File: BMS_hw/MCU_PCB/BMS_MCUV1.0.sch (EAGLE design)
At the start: 37 parts, among them IC2 SST25VF020B804ISA, Q1 CRYSTALS-GND-LID-IQXC-42

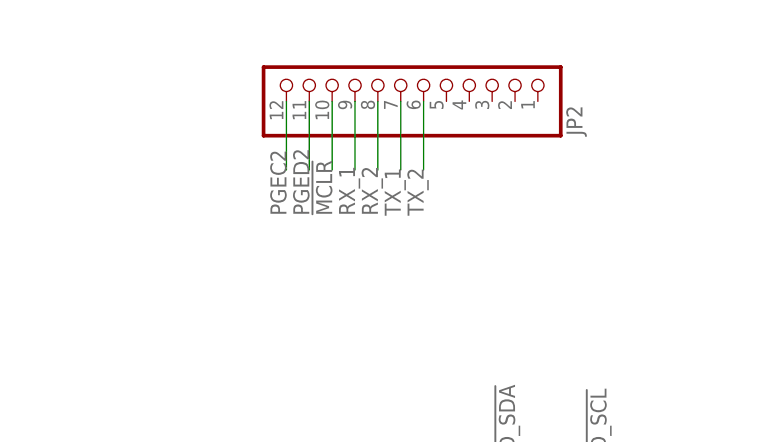
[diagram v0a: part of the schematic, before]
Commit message: afe mcu schematic updated
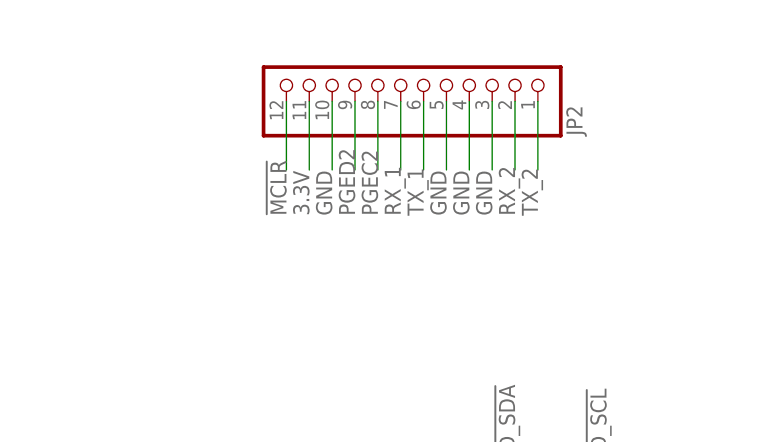
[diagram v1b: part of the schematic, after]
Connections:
- net !MCLR: now also JP2.12; no longer JP2.10
- net 3.3V: now also JP2.11
- net GND: now also JP2.10, JP2.3, JP2.4, JP2.5
- net PGEC2: now also JP2.8; no longer JP2.12
- net PGED2: now also JP2.9; no longer JP2.11
- net RX_1: now also JP2.7; no longer JP2.9
- net RX_2: now also JP2.2; no longer JP2.8
- net TX_1: now also JP2.6; no longer JP2.7
- net TX_2: now also JP2.1; no longer JP2.6
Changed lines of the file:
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@@
 <pinref part="GND13" gate="1" pin="GND"/>
+</segment>
+<segment>
+<pinref part="JP2" gate="G$1" pin="10"/>
+<wire x1="317.5" y1="243.84" x2="317.5" y2="236.22" width="0.1524" layer="91"/>
+<label x="317.5" y="231.14" size="1.778" layer="95" font="vector" ratio="12" rot="R90"/>
+</segment>
+<segment>
+<pinref part="JP2" gate="G$1" pin="5"/>
+<wire x1="330.2" y1="243.84" x2="330.2" y2="236.22" width="0.1524" layer="91"/>
+<label x="330.2" y="231.14" size="1.778" layer="95" rot="R90"/>
+</segment>
+<segment>
+<pinref part="JP2" gate="G$1" pin="4"/>
+<wire x1="332.74" y1="243.84" x2="332.74" y2="236.22" width="0.1524" layer="91"/>
+<label x="332.74" y="231.14" size="1.778" layer="95" rot="R90"/>
+</segment>
+<segment>
+<pinref part="JP2" gate="G$1" pin="3"/>
+<wire x1="335.28" y1="243.84" x2="335.28" y2="236.22" width="0.1524" layer="91"/>
+<label x="335.28" y="231.14" size="1.778" layer="95" rot="R90"/>
 </segment>
 </net>
@@
 <wire x1="228.6" y1="210.82" x2="220.98" y2="210.82" width="0.1524" layer="91"/>
 <label x="215.9" y="210.82" size="1.778" layer="95" font="vector" ratio="12"/>
+</segment>
+<segment>
+<pinref part="JP2" gate="G$1" pin="11"/>
+<wire x1="314.96" y1="243.84" x2="314.96" y2="236.22" width="0.1524" layer="91"/>
+<label x="314.96" y="231.14" size="1.778" layer="95" font="vector" ratio="12" rot="R90"/>
 </segment>
 </net>
@@
 </segment>
 <segment>
-<pinref part="JP2" gate="G$1" pin="10"/>
-<wire x1="317.5" y1="243.84" x2="317.5" y2="236.22" width="0.1524" layer="91"/>
-<label x="317.5" y="231.14" size="1.778" layer="95" font="vector" ratio="12" rot="R90"/>
+<pinref part="JP2" gate="G$1" pin="12"/>
+<wire x1="312.42" y1="243.84" x2="312.42" y2="236.22" width="0.1524" layer="91"/>
+<label x="312.42" y="231.14" size="1.778" layer="95" font="vector" ratio="12" rot="R90"/>
 </segment>
 </net>
@@
 </segment>
 <segment>
-<pinref part="JP2" gate="G$1" pin="9"/>
-<wire x1="320.04" y1="243.84" x2="320.04" y2="236.22" width="0.1524" layer="91"/>
-<label x="320.04" y="231.14" size="1.778" layer="95" font="vector" ratio="12" rot="R90"/>
+<pinref part="JP2" gate="G$1" pin="7"/>
+<wire x1="325.12" y1="243.84" x2="325.12" y2="236.22" width="0.1524" layer="91"/>
+<label x="325.12" y="231.14" size="1.778" layer="95" font="vector" ratio="12" rot="R90"/>
 </segment>
 </net>
@@
 </segment>
 <segment>
+<pinref part="JP2" gate="G$1" pin="1"/>
+<wire x1="340.36" y1="243.84" x2="340.36" y2="236.22" width="0.1524" layer="91"/>
+<label x="340.36" y="231.14" size="1.778" layer="95" rot="R90"/>
+</segment>
+</net>
+<net name="N$73" class="0">
+<segment>
+<pinref part="MCU2" gate="G$1" pin="OA3IN+/AN8/C3IN1+/C3IN3-/RPC2/PMA13/RC2"/>
+<wire x1="35.56" y1="157.48" x2="33.02" y2="157.48" width="0.1524" layer="91"/>
+</segment>
+</net>
+<net name="TX_1" class="0">
+<segment>
+<pinref part="MCU2" gate="G$1" pin="RPB15/PMD7/RB15"/>
+<wire x1="35.56" y1="170.18" x2="33.02" y2="170.18" width="0.1524" layer="91"/>
+<label x="27.94" y="170.18" size="1.778" layer="95" font="vector" ratio="12"/>
+</segment>
+<segment>
 <pinref part="JP2" gate="G$1" pin="6"/>
 <wire x1="327.66" y1="243.84" x2="327.66" y2="236.22" width="0.1524" layer="91"/>
 <label x="327.66" y="231.14" size="1.778" layer="95" font="vector" ratio="12" rot="R90"/>
-</segment>
-</net>
-<net name="N$73" class="0">
-<segment>
-<pinref part="MCU2" gate="G$1" pin="OA3IN+/AN8/C3IN1+/C3IN3-/RPC2/PMA13/RC2"/>
-<wire x1="35.56" y1="157.48" x2="33.02" y2="157.48" width="0.1524" layer="91"/>
-</segment>
-</net>
-<net name="TX_1" class="0">
-<segment>
-<pinref part="MCU2" gate="G$1" pin="RPB15/PMD7/RB15"/>
-<wire x1="35.56" y1="170.18" x2="33.02" y2="170.18" width="0.1524" layer="91"/>
-<label x="27.94" y="170.18" size="1.778" layer="95" font="vector" ratio="12"/>
-</segment>
-<segment>
-<pinref part="JP2" gate="G$1" pin="7"/>
-<wire x1="325.12" y1="243.84" x2="325.12" y2="236.22" width="0.1524" layer="91"/>
-<label x="325.12" y="231.14" size="1.778" layer="95" font="vector" ratio="12" rot="R90"/>
 </segment>
 </net>
@@
 </segment>
 <segment>
-<pinref part="JP2" gate="G$1" pin="12"/>
-<wire x1="312.42" y1="243.84" x2="312.42" y2="236.22" width="0.1524" layer="91"/>
-<label x="312.42" y="231.14" size="1.778" layer="95" font="vector" ratio="12" rot="R90"/>
+<pinref part="JP2" gate="G$1" pin="8"/>
+<wire x1="322.58" y1="243.84" x2="322.58" y2="236.22" width="0.1524" layer="91"/>
+<label x="322.58" y="231.14" size="1.778" layer="95" font="vector" ratio="12" rot="R90"/>
 </segment>
 </net>
@@
 </segment>
 <segment>
-<pinref part="JP2" gate="G$1" pin="11"/>
-<wire x1="314.96" y1="243.84" x2="314.96" y2="236.22" width="0.1524" layer="91"/>
-<label x="314.96" y="231.14" size="1.778" layer="95" font="vector" ratio="12" rot="R90"/>
+<pinref part="JP2" gate="G$1" pin="9"/>
+<wire x1="320.04" y1="243.84" x2="320.04" y2="236.22" width="0.1524" layer="91"/>
+<label x="320.04" y="231.14" size="1.778" layer="95" font="vector" ratio="12" rot="R90"/>
 </segment>
 </net>
@@
 </segment>
 <segment>
-<pinref part="JP2" gate="G$1" pin="8"/>
-<wire x1="322.58" y1="243.84" x2="322.58" y2="236.22" width="0.1524" layer="91"/>
-<label x="322.58" y="231.14" size="1.778" layer="95" font="vector" ratio="12" rot="R90"/>
-</segment>
-</net>
+<pinref part="JP2" gate="G$1" pin="2"/>
+<wire x1="337.82" y1="243.84" x2="337.82" y2="236.22" width="0.1524" layer="91"/>
+<label x="337.82" y="231.14" size="1.778" layer="95" rot="R90"/>
+</segment>
+</net>

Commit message: afe ver 1.1 added@itt@20
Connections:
- new net CHG_GATE: JP5.9, MCU2.AN14/RPE14/PMA1/RE14
- new net DSG_GATE: JP5.8, MCU2.RPB4/PMA8/RB4
- new net FLOUT: JP1.7, MCU2.AN9/RPA11/RA11
- new net KEY-IN: JP1.13, MCU2.OA2OUT/AN0/C2IN4-/C4IN3-/RPA0/RA0
- new net PCHG_GATE: JP5.10, MCU2.AN13/C3IN2-/PMA10/RE13
- new net RDD: JP5.12
- new net SGNL1: JP5.11
- net 3.3V: now also JP5.13
- net 5V: now also JP1.10, JP1.11
- net GND: now also JP1.12, JP1.8, JP1.9, JP5.14, JP5.15
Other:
- moved on the sheet: C13, C14, C7, IC2, JP2

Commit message: itt@21
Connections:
- net 3.3V: now also JP2.2; no longer JP2.11
- net GND: now also JP2.1, JP2.6, JP2.9; no longer JP2.10, JP2.4, JP2.5
- net PGEC2: now also JP2.10; no longer JP2.8
- net PGED2: now also JP2.11; no longer JP2.9
- net RX_1: now also JP2.8; no longer JP2.7
- net RX_2: now also JP2.5; no longer JP2.2
- net TX_1: now also JP2.7; no longer JP2.6
- net TX_2: now also JP2.4; no longer JP2.1
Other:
- moved on the sheet: JP2
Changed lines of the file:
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@@
 <text x="289.56" y="12.7" size="2.1844" layer="94">Greenfuel Energy Solutions Pvt. Ltd.</text>
 <text x="228.6" y="182.88" size="1.778" layer="94" font="vector" ratio="12">&gt;Aux connectors</text>
+<text x="276.86" y="233.68" size="1.778" layer="94" font="vector" ratio="12">&gt;Programming/Debugging/UART communication ribbon</text>
 </plain>
 <instances>
@@
 <attribute name="VALUE" x="10.16" y="104.14" size="1.778" layer="96"/>
 </instance>
-<instance part="JP2" gate="G$1" x="299.72" y="215.9" rot="MR90">
-<attribute name="NAME" x="315.595" y="209.55" size="1.778" layer="95" rot="MR90"/>
-<attribute name="VALUE" x="279.4" y="209.55" size="1.778" layer="96" rot="MR90"/>
+<instance part="JP2" gate="G$1" x="297.18" y="226.06" rot="MR90">
+<attribute name="NAME" x="297.18" y="228.6" size="1.778" layer="95" font="vector" ratio="12" rot="MR0"/>
+<attribute name="VALUE" x="276.86" y="219.71" size="1.778" layer="96" rot="MR90"/>
 </instance>
 </instances>
@@
 </segment>
 <segment>
-<pinref part="JP2" gate="G$1" pin="10"/>
-<wire x1="289.56" y1="213.36" x2="289.56" y2="205.74" width="0.1524" layer="91"/>
-<label x="289.56" y="200.66" size="1.778" layer="95" font="vector" ratio="12" rot="R90"/>
-</segment>
-<segment>
-<pinref part="JP2" gate="G$1" pin="5"/>
-<wire x1="302.26" y1="213.36" x2="302.26" y2="205.74" width="0.1524" layer="91"/>
-<label x="302.26" y="200.66" size="1.778" layer="95" font="vector" ratio="12" rot="R90"/>
-</segment>
-<segment>
-<pinref part="JP2" gate="G$1" pin="4"/>
-<wire x1="304.8" y1="213.36" x2="304.8" y2="205.74" width="0.1524" layer="91"/>
-<label x="304.8" y="200.66" size="1.778" layer="95" font="vector" ratio="12" rot="R90"/>
-</segment>
-<segment>
-<pinref part="JP2" gate="G$1" pin="3"/>
-<wire x1="307.34" y1="213.36" x2="307.34" y2="205.74" width="0.1524" layer="91"/>
-<label x="307.34" y="200.66" size="1.778" layer="95" font="vector" ratio="12" rot="R90"/>
-</segment>
-<segment>
 <pinref part="JP5" gate="A" pin="14"/>
 <wire x1="228.6" y1="193.04" x2="220.98" y2="193.04" width="0.1524" layer="91"/>
@@
 <pinref part="C13" gate="G$1" pin="2"/>
 <wire x1="302.26" y1="118.11" x2="302.26" y2="119.38" width="0.1524" layer="91"/>
+</segment>
+<segment>
+<pinref part="JP2" gate="G$1" pin="9"/>
+<wire x1="289.56" y1="223.52" x2="289.56" y2="215.9" width="0.1524" layer="91"/>
+<label x="289.56" y="210.82" size="1.778" layer="95" font="vector" ratio="12" rot="R90"/>
+</segment>
+<segment>
+<pinref part="JP2" gate="G$1" pin="6"/>
+<wire x1="297.18" y1="223.52" x2="297.18" y2="215.9" width="0.1524" layer="91"/>
+<label x="297.18" y="210.82" size="1.778" layer="95" font="vector" ratio="12" rot="R90"/>
+</segment>
+<segment>
+<pinref part="JP2" gate="G$1" pin="3"/>
+<wire x1="304.8" y1="223.52" x2="304.8" y2="215.9" width="0.1524" layer="91"/>
+<label x="304.8" y="210.82" size="1.778" layer="95" font="vector" ratio="12" rot="R90"/>
+</segment>
+<segment>
+<pinref part="JP2" gate="G$1" pin="1"/>
+<wire x1="309.88" y1="223.52" x2="309.88" y2="215.9" width="0.1524" layer="91"/>
+<label x="309.88" y="210.82" size="1.778" layer="95" font="vector" ratio="12" rot="R90"/>
 </segment>
 </net>
@@
 </segment>
 <segment>
-<pinref part="JP2" gate="G$1" pin="11"/>
-<wire x1="287.02" y1="213.36" x2="287.02" y2="205.74" width="0.1524" layer="91"/>
-<label x="287.02" y="200.66" size="1.778" layer="95" font="vector" ratio="12" rot="R90"/>
-</segment>
-<segment>
 <pinref part="JP5" gate="A" pin="13"/>
 <wire x1="228.6" y1="195.58" x2="220.98" y2="195.58" width="0.1524" layer="91"/>
 <label x="215.9" y="195.58" size="1.778" layer="95" font="vector" ratio="12"/>
+</segment>
+<segment>
+<pinref part="JP2" gate="G$1" pin="2"/>
+<wire x1="307.34" y1="223.52" x2="307.34" y2="215.9" width="0.1524" layer="91"/>
+<label x="307.34" y="210.82" size="1.778" layer="95" font="vector" ratio="12" rot="R90"/>
 </segment>
 </net>
@@
 <segment>
 <pinref part="JP2" gate="G$1" pin="12"/>
-<wire x1="284.48" y1="213.36" x2="284.48" y2="205.74" width="0.1524" layer="91"/>
-<label x="284.48" y="200.66" size="1.778" layer="95" font="vector" ratio="12" rot="R90"/>
+<wire x1="281.94" y1="223.52" x2="281.94" y2="215.9" width="0.1524" layer="91"/>
+<label x="281.94" y="210.82" size="1.778" layer="95" font="vector" ratio="12" rot="R90"/>
 </segment>
 </net>
@@
 </segment>
 <segment>
-<pinref part="JP2" gate="G$1" pin="7"/>
-<wire x1="297.18" y1="213.36" x2="297.18" y2="205.74" width="0.1524" layer="91"/>
-<label x="297.18" y="200.66" size="1.778" layer="95" font="vector" ratio="12" rot="R90"/>
+<pinref part="JP2" gate="G$1" pin="8"/>
+<wire x1="292.1" y1="223.52" x2="292.1" y2="215.9" width="0.1524" layer="91"/>
+<label x="292.1" y="210.82" size="1.778" layer="95" font="vector" ratio="12" rot="R90"/>
 </segment>
 </net>
@@
 </segment>
 <segment>
-<pinref part="JP2" gate="G$1" pin="1"/>
-<wire x1="312.42" y1="213.36" x2="312.42" y2="205.74" width="0.1524" layer="91"/>
-<label x="312.42" y="200.66" size="1.778" layer="95" font="vector" ratio="12" rot="R90"/>
+<pinref part="JP2" gate="G$1" pin="4"/>
+<wire x1="302.26" y1="223.52" x2="302.26" y2="215.9" width="0.1524" layer="91"/>
+<label x="302.26" y="210.82" size="1.778" layer="95" font="vector" ratio="12" rot="R90"/>
 </segment>
 </net>
@@
 </segment>
 <segment>
-<pinref part="JP2" gate="G$1" pin="6"/>
-<wire x1="299.72" y1="213.36" x2="299.72" y2="205.74" width="0.1524" layer="91"/>
-<label x="299.72" y="200.66" size="1.778" layer="95" font="vector" ratio="12" rot="R90"/>
+<pinref part="JP2" gate="G$1" pin="7"/>
+<wire x1="294.64" y1="223.52" x2="294.64" y2="215.9" width="0.1524" layer="91"/>
+<label x="294.64" y="210.82" size="1.778" layer="95" font="vector" ratio="12" rot="R90"/>
 </segment>
 </net>
@@
 </segment>
 <segment>
-<pinref part="JP2" gate="G$1" pin="8"/>
-<wire x1="294.64" y1="213.36" x2="294.64" y2="205.74" width="0.1524" layer="91"/>
-<label x="294.64" y="200.66" size="1.778" layer="95" font="vector" ratio="12" rot="R90"/>
+<pinref part="JP2" gate="G$1" pin="10"/>
+<wire x1="287.02" y1="223.52" x2="287.02" y2="215.9" width="0.1524" layer="91"/>
+<label x="287.02" y="208.28" size="1.778" layer="95" font="vector" ratio="12" rot="R90"/>
 </segment>
 </net>
@@
 </segment>
 <segment>
-<pinref part="JP2" gate="G$1" pin="9"/>
-<wire x1="292.1" y1="213.36" x2="292.1" y2="205.74" width="0.1524" layer="91"/>
-<label x="292.1" y="200.66" size="1.778" layer="95" font="vector" ratio="12" rot="R90"/>
+<pinref part="JP2" gate="G$1" pin="11"/>
+<wire x1="284.48" y1="223.52" x2="284.48" y2="215.9" width="0.1524" layer="91"/>
+<label x="284.48" y="208.28" size="1.778" layer="95" font="vector" ratio="12" rot="R90"/>
 </segment>
 </net>
@@
 </segment>
 <segment>
-<pinref part="JP2" gate="G$1" pin="2"/>
-<wire x1="309.88" y1="213.36" x2="309.88" y2="205.74" width="0.1524" layer="91"/>
-<label x="309.88" y="200.66" size="1.778" layer="95" font="vector" ratio="12" rot="R90"/>
-</segment>
-</net>
+<pinref part="JP2" gate="G$1" pin="5"/>
+<wire x1="299.72" y1="223.52" x2="299.72" y2="215.9" width="0.1524" layer="91"/>
+<label x="299.72" y="210.82" size="1.778" layer="95" font="vector" ratio="12" rot="R90"/>
+</segment>
+</net>

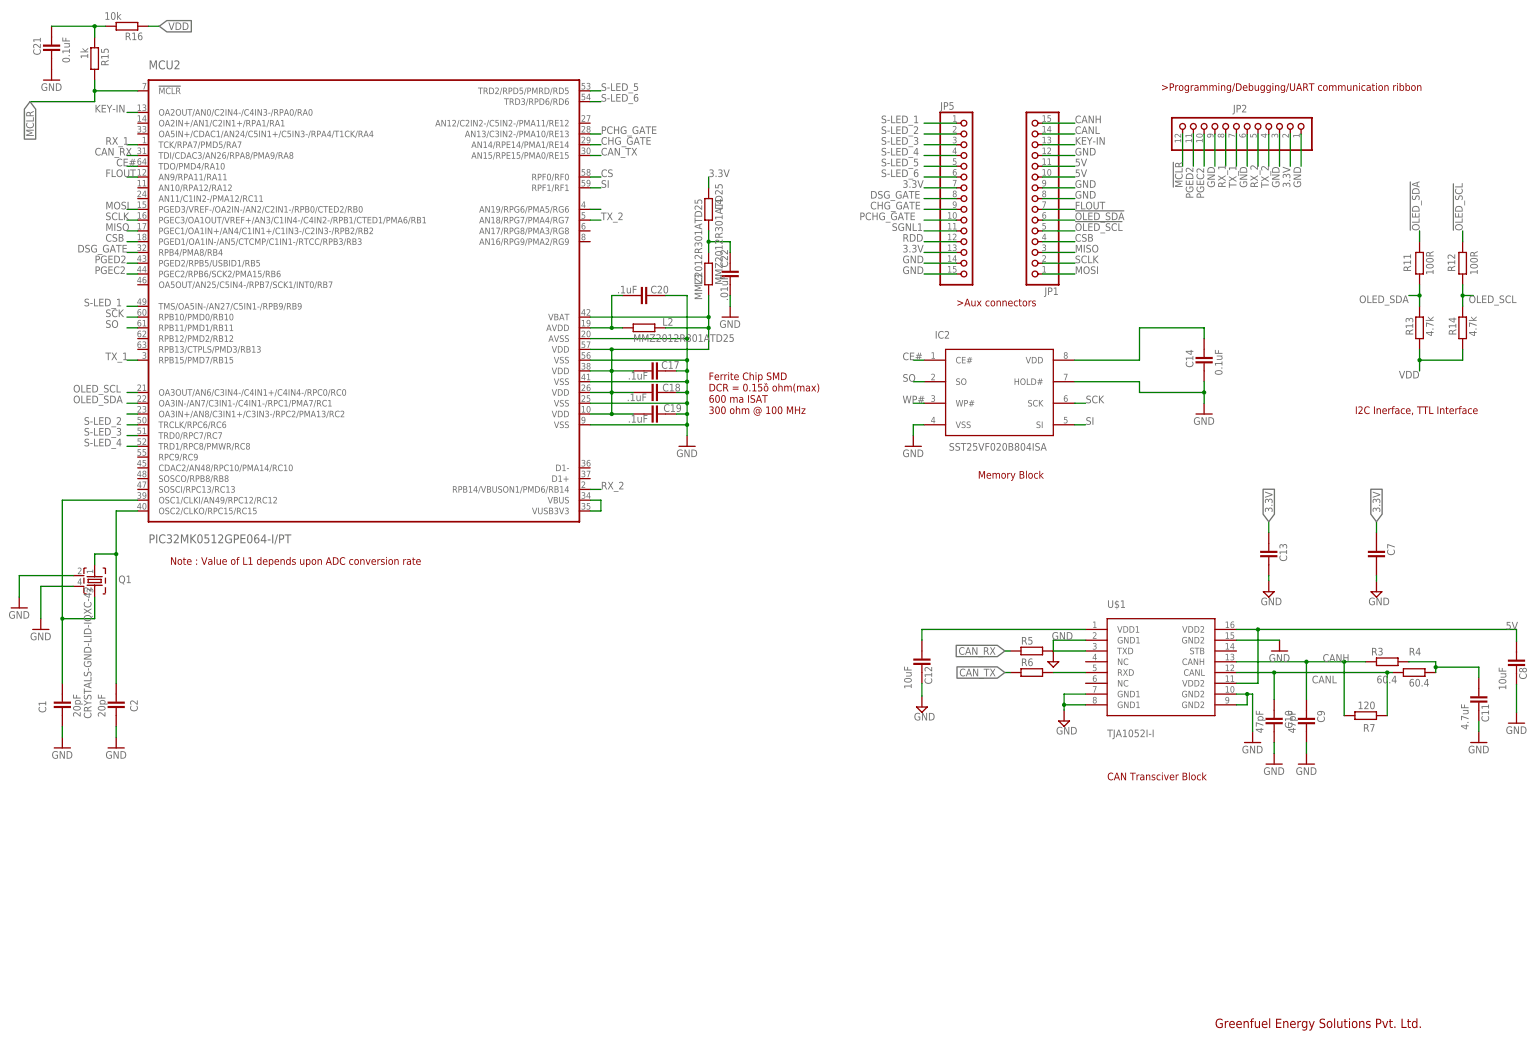
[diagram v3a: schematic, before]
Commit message: replace part with fod8384 with tlp152 added datasheet in doc folder
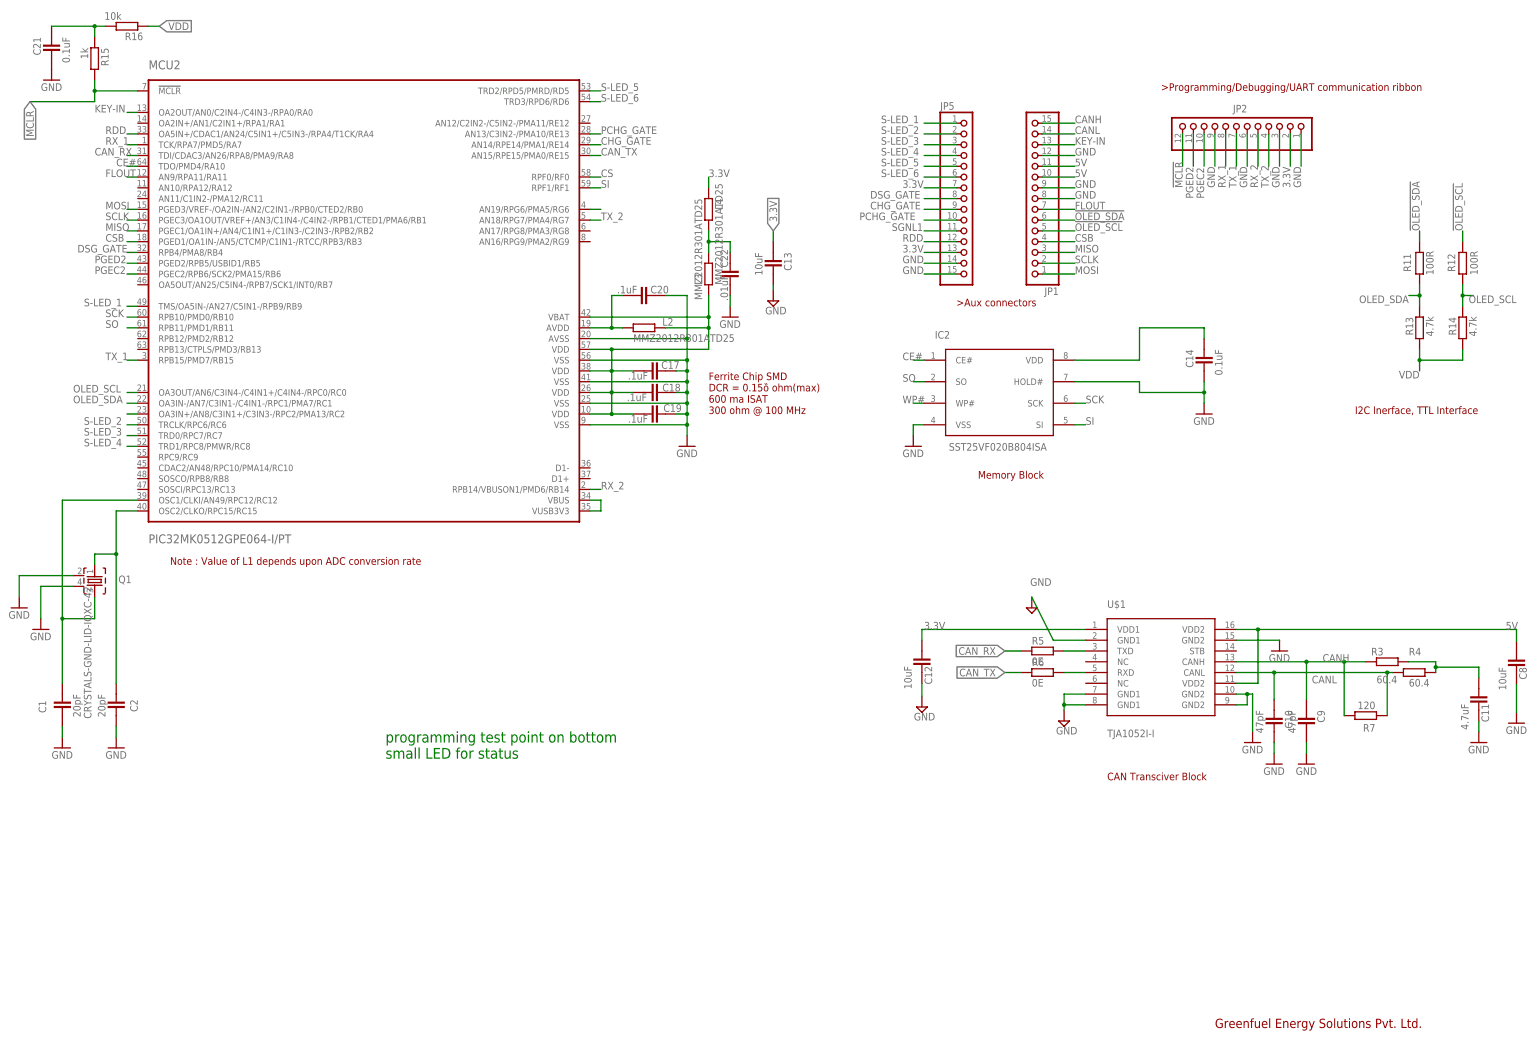
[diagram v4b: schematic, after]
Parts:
- removed C7: (no value), ipc-7351-capacitor:CAPACITOR_0402
- C13: value (none) -> 10uF
- R5, R6: value (none) -> 0E
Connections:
- net 3.3V: now also C12.1, U$1.VDD1; no longer C7.1
- net GND: no longer C7.2
- net N$3: now also R5.2, U$1.TXD; no longer C12.1, U$1.VDD1
- net N$7: no longer R5.2, U$1.TXD
- net RDD: now also MCU2.OA5IN+/CDAC1/AN24/C5IN1+/C5IN3-/RPA4/T1CK/RA4
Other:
- note added: "programming test point on bottom small LED for status"
- moved on the sheet: C13, R5, R6
